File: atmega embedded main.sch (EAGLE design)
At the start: 148 parts, among them K1 SWITCH, K10 SWITCH, K11 SWITCH, K12 SWITCH, K13 SWITCH, K14 SWITCH, K15 SWITCH, K16 SWITCH, K17 SWITCH, K18 SWITCH, K19 SWITCH, K2 SWITCH, K20 SWITCH, K21 SWITCH, K22 SWITCH, K23 SWITCH, K24 SWITCH, K25 SWITCH, K26 SWITCH, K27 SWITCH, K28 SWITCH, K29 SWITCH, K3 SWITCH, K30 SWITCH, K31 SWITCH, K32 SWITCH, K33 SWITCH, K34 SWITCH, K35 SWITCH, K36 SWITCH, K37 SWITCH, K38 SWITCH, K39 SWITCH, K4 SWITCH, K40 SWITCH, K41 SWITCH, K42 SWITCH, K43 SWITCH, K44 SWITCH, K45 SWITCH, K46 SWITCH, K47 SWITCH, K48 SWITCH, K49 SWITCH, K5 SWITCH, K50 SWITCH, K51 SWITCH, K52 SWITCH, K53 SWITCH, K54 SWITCH, K55 SWITCH, K56 SWITCH, K57 SWITCH, K58 SWITCH, K59 SWITCH, K6 SWITCH, K60 SWITCH, K61 SWITCH, K62 SWITCH, K63 SWITCH, K64 SWITCH, K65 SWITCH, K66 SWITCH, K7 SWITCH, K8 SWITCH, K9 SWITCH, U1 ATMEGA32U4-AU, X1 XTAL_GND

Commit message: Replaced chip with Atmege328p and made some other adjustments to the schematic
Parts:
- removed D45: (no value), adafruit:DIODEDO-1N4148
- removed D63: (no value), adafruit:DIODESMA
- removed K60: SWITCH, keyboard_switch:SWITCH
- added C10, C9: 22p, adafruit:C-USC0805
- added CN2: (no value), adafruit:USBMINIB
- added D29: (no value), adafruit:DIODESMA
- added IC1: ATMEGA328PROUND, atmega328:ATMEGA328PROUND
- added R5: 10K, adafruit:R-US_M0805
- added R6, R7: 22, adafruit:R-US_M0805
- added SW2: (no value), adafruit:SWITCH_PUSHBUTTONSOFTTOUCHSMD_SJ
- added X2: XTAL_GND, adafruit:XTAL-4-3225
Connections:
- removed net N$43: D45.C, K24.P$2
- removed net N$65: D63.C, K60.P$2
- removed net N$80: D15.C, K47.P$2
- new net D+: CN2.D+, IC1.(PCI8/ADC0)PC0, R6.1, R6.2
- new net D-: CN2.D-, R7.2
- new net N$15: IC1.PC6(/RESET/PCI14), R5.2, SW2.P$2
- new net N$16: C9.1, IC1.PB6(XTAL1/TOSC1/PCI6), X2.X1
- new net N$17: C10.1, IC1.PB7(XTAL2/TOSC2/PCI7), X2.X2
- new net N$19: D15.C, K24.P$2
- new net N$20: D29.C, K47.P$2
- new net N$21: IC1.(PCI9/ADC1)PC1, R7.1
- new net N$22: CN2.ID
- net COL10: now also K62.P$1
- net COL13: no longer K60.P$1
- net COL14: no longer K47.P$1
- net COL3: no longer K24.P$1
- net COL6: now also K47.P$1
- net COL8: now also K24.P$1
- net COL9: no longer K62.P$1
- net GND: now also C10.2, C9.2, CN2.GND, IC1.AGND, IC1.GND, SW2.P$1, X2.G2
- net ROW1: now also D15.A, D29.A
- net ROW2: no longer D45.A, D63.A
- net ROW4: no longer D15.A
- net VCC: now also CN2.VBUS, IC1.AREF, IC1.AVCC, IC1.VCC, R5.1
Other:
- note added: "Floating ID pin means USB-B device"
- note added: "Reject, wrong chip"
- note added: "TODO: Regulate VCC with some condensers or something."
- moved on the sheet: C1, C2, C3, C4, C5, C6, C7, C8, CN1, D10, D11, D12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

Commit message: Added an alternative wiring with fake rows for a chip with fewer pins
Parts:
- added D100, D101, D102, D103, D104, D105, D106, D107, D108, D109, D110, D111, D112, D113, D114, D115, D116, D117, D118, D119, D120, D121, D122, D123, D124, D125, D126, D127, D128, D129, D130, D98, D99: (no value), adafruit:DIODESMA
- added D45, D63, D68, D69, D70, D71, D72, D73, D74, D75, D76, D77, D78, D79, D80, D81, D82, D83, D84, D85, D86, D87, D88, D89, D90, D91, D92, D93, D94, D95, D96, D97: (no value), adafruit:DIODEDO-1N4148
- added K100, K101, K102, K103, K104, K105, K106, K107, K108, K109, K110, K111, K112, K113, K114, K115, K116, K117, K118, K119, K120, K121, K122, K123, K124, K125, K126, K127, K128, K129, K130, K60, K67, K68, K69, K70, K71, K72, K73, K74, K75, K76, K77, K78, K79, K80, K81, K82, K83, K84, K85, K86, K87, K88, K89, K90, K91, K92, K93, K94, K95, K96, K97, K98, K99: SWITCH, keyboard_switch:SWITCH
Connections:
- new net N$100: D71.C, K71.P$2
- new net N$101: D74.C, K78.P$2
- new net N$102: D116.C, K98.P$1
- new net N$103: D117.C, K105.P$1
- new net N$104: D95.C, K85.P$2
- new net N$105: D94.C, K91.P$2
- new net N$106: D104.C, K128.P$2
- new net N$107: D86.C, K97.P$2
- new net N$108: D93.C, K90.P$2
- new net N$109: D92.C, K84.P$2
- new net N$110: D75.C, K77.P$2
- new net N$111: D115.C, K104.P$2
- new net N$112: D127.C, K123.P$2
- new net N$113: D111.C, K124.P$2
- new net N$114: D126.C, K121.P$2
- new net N$115: D120.C, K120.P$2
- new net N$116: D128.C, K117.P$2
- new net N$118: D114.C, K127.P$2
- new net N$119: D113.C, K126.P$2
- new net N$120: D112.C, K125.P$2
- new net N$121: D119.C, K119.P$2
- new net N$123: D99.C, K99.P$2
- new net N$124: D100.C, K100.P$2
- new net N$125: D101.C, K101.P$2
- new net N$126: D102.C, K102.P$2
- new net N$127: D103.C, K103.P$2
- new net N$130: D124.C, K116.P$2
- new net N$131: D123.C, K115.P$2
- new net N$132: D122.C, K114.P$2
- new net N$133: D121.C, K113.P$2
- new net N$134: D118.C, K112.P$2
- new net N$135: D109.C, K106.P$2
- new net N$136: D108.C, K107.P$2
- new net N$137: D107.C, K108.P$2
- new net N$138: D106.C, K109.P$2
- new net N$139: D105.C, K110.P$2
- new net N$141: D63.C, K67.P$2
- new net N$142: D125.C, K122.P$2
- new net N$143: D129.C, K129.P$1
- new net N$144: D130.C, K130.P$2
- new net N$151: D82.C, K93.P$1
- new net N$152: D81.C, K87.P$1
- new net N$153: D80.C, K80.P$1
- new net N$154: D105.A, D106.A, D107.A, D108.A, D109.A
- new net N$155: D100.A, D101.A, D102.A, D103.A, D99.A
- new net N$160: D87.A, D90.A, D93.A, D94.A
- new net N$161: D72.C, K72.P$2
- new net N$162: D73.C, K79.P$2
- new net N$163: D96.C, K86.P$2
- new net N$164: D97.C, K92.P$2
- new net N$23: D45.C, K60.P$1
- new net N$24: D83.C, K94.P$2
- new net N$25: D79.C, K73.P$1
- new net N$26: D118.A, D121.A, D122.A, D123.A, D124.A
- new net N$27: D98.C, K118.P$1
- new net N$28: D110.C, K111.P$1
- new net N$35: D78.C, K74.P$2
- new net N$43: D77.C, K75.P$2
- new net N$64: D68.C, K68.P$2
- new net N$65: D89.C, K82.P$2
- new net N$72: D88.C, K81.P$2
- new net N$80: D87.C, K88.P$2
- new net N$92: D84.C, K95.P$2
- new net N$93: D85.C, K96.P$2
- new net N$94: D90.C, K89.P$2
- new net N$95: D91.C, K83.P$2
- new net N$96: D76.C, K76.P$2
- new net N$97: D69.C, K69.P$2
- new net N$98: D70.C, K70.P$2
- new net ROW6: D104.A, D115.A, D127.A, D128.A, D45.A, D79.A, D80.A, D81.A, D82.A
- new net ROW7: D110.A, D116.A, D117.A, D72.A, D73.A, D96.A, D97.A, D98.A
- net COL10: now also K100.P$1, K107.P$1, K111.P$2, K113.P$1, K120.P$1, K124.P$1, K128.P$1
- net COL11: now also K101.P$1, K105.P$2, K108.P$1, K114.P$1, K121.P$1, K123.P$1, K125.P$1
- net COL12: now also K102.P$1, K109.P$1, K115.P$1, K117.P$1, K122.P$1, K126.P$1, K98.P$2
- net COL13: now also K103.P$1, K104.P$1, K110.P$1, K116.P$1, K127.P$1
- net COL2: now also K60.P$2, K67.P$1, K74.P$1, K81.P$1, K88.P$1, K94.P$1
- net COL3: now also K68.P$1, K72.P$1, K73.P$2, K75.P$1, K82.P$1, K95.P$1
- net COL4: now also K69.P$1, K76.P$1, K79.P$1, K80.P$2, K83.P$1, K89.P$1, K96.P$1
- net COL5: now also K70.P$1, K77.P$1, K84.P$1, K86.P$1, K87.P$2, K90.P$1, K97.P$1
- net COL6: now also K130.P$1, K71.P$1, K78.P$1, K85.P$1, K91.P$1, K92.P$1, K93.P$2
- net COL9: now also K106.P$1, K112.P$1, K118.P$2, K119.P$1, K129.P$2, K99.P$1
- net ROW1: now also D63.A, D68.A, D69.A, D70.A, D71.A
- net ROW2: now also D74.A, D75.A, D76.A, D77.A, D78.A
- net ROW3: now also D88.A, D89.A, D91.A, D92.A, D95.A
- net ROW4: now also D119.A, D120.A, D125.A, D126.A
- net ROW5: now also D111.A, D112.A, D113.A, D114.A, D129.A, D130.A, D83.A, D84.A, D85.A, D86.A
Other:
- moved on the sheet: C1, C2, C8, CN1, R1, R2, R3, R4, SW1, U1, X1

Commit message: Traced stuff
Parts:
- removed C1, C2: 22p, adafruit:C-USC0805
- removed C8: 1u, adafruit:C-USC0805
- removed CN1, CN2: (no value), adafruit:USBMINIB
- removed D1, D2, D22, D23, D24, D25, D26, D27, D28, D3, D30, D31, D32, D33, D34, D35, D36, D4, D42, D43, D44, D46, D47, D48, D49, D5, D50, D51, D52, D53, D6, D7: (no value), adafruit:DIODEDO-1N4148
- removed D10, D11, D12, D13, D14, D15, D16, D17, D18, D19, D20, D21, D29, D37, D38, D39, D40, D41, D54, D55, D56, D57, D58, D59, D60, D61, D62, D64, D65, D66, D67, D8, D9: (no value), adafruit:DIODESMA
- removed K1, K10, K11, K12, K13, K14, K15, K16, K17, K18, K19, K2, K20, K21, K22, K23, K24, K25, K26, K27, K28, K29, K3, K30, K31, K32, K33, K34, K35, K36, K37, K38, K39, K4, K40, K41, K42, K43, K44, K45, K46, K47, K48, K49, K5, K50, K51, K52, K53, K54, K55, K56, K57, K58, K59, K6, K61, K62, K63, K64, K65, K66, K7, K8, K9: SWITCH, keyboard_switch:SWITCH
- removed R1, R2: 10K, adafruit:R-US_M0805
- removed R3, R4: 22, adafruit:R-US_M0805
- removed SW1, SW2: (no value), adafruit:SWITCH_PUSHBUTTONSOFTTOUCHSMD_SJ
- removed X1, X2: XTAL_GND, adafruit:XTAL-4-3225
- added Q1: (no value), crystal:CRYSTALHC49S
- added S1: (no value), switch-omron:10-XX
- D45, D63, D68, D69, D70, D71, D72, D73, D74, D75, D76, D77, D78, D79, D80, D81, D82, D83, D84, D85, D86, D87, D88, D89, D90, D91, D92, D93, D94, D95, D96, D97: device adafruit:DIODEDO-1N4148 -> adafruit:DIODESMA
- U1: value ATMEGA32U4-AU -> (none); device adafruit:ATMEGA32U4-AU -> microusb:USB""
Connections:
- removed net COL11: K101.P$1, K105.P$2, K108.P$1, K114.P$1, K121.P$1, K123.P$1, K125.P$1, K37.P$1, K44.P$1, K51.P$1, K58.P$1, K63.P$1, U1.PB7(OC0A/OC1C/RTS)
- removed net COL12: K102.P$1, K109.P$1, K115.P$1, K117.P$1, K122.P$1, K126.P$1, K38.P$1, K45.P$1, K52.P$1, K59.P$1, K64.P$1, K98.P$2, U1.PF7(ADC7(TDI)
- removed net COL13: K103.P$1, K104.P$1, K110.P$1, K116.P$1, K127.P$1, K39.P$1, K46.P$1, K53.P$1, K65.P$1, U1.PF6(ADC6/TDO)
- removed net COL14: K40.P$1, K54.P$1, K61.P$1, K66.P$1, U1.PF5(ADC5/TMS)
- removed net N$1 (its old number): C1.1, U1.XTAL1, X1.X1
- removed net N$100: D71.C, K71.P$2
- removed net N$101: D74.C, K78.P$2
- removed net N$102: D116.C, K98.P$1
- removed net N$103: D117.C, K105.P$1
- removed net N$104: D95.C, K85.P$2
- removed net N$105: D94.C, K91.P$2
- removed net N$107: D86.C, K97.P$2
- removed net N$108: D93.C, K90.P$2
- removed net N$109: D92.C, K84.P$2
- removed net N$110: D75.C, K77.P$2
- removed net N$113: D111.C, K124.P$2
- removed net N$114: D126.C, K121.P$2
- removed net N$115: D120.C, K120.P$2
- removed net N$118: D114.C, K127.P$2
- removed net N$119: D113.C, K126.P$2
- removed net N$120: D112.C, K125.P$2
- removed net N$121: D119.C, K119.P$2
- removed net N$123: D99.C, K99.P$2
- removed net N$124: D100.C, K100.P$2
- removed net N$125: D101.C, K101.P$2
- removed net N$126: D102.C, K102.P$2
- removed net N$127: D103.C, K103.P$2
- removed net N$130: D124.C, K116.P$2
- removed net N$131: D123.C, K115.P$2
- removed net N$132: D122.C, K114.P$2
- removed net N$133: D121.C, K113.P$2
- removed net N$134: D118.C, K112.P$2
- removed net N$135: D109.C, K106.P$2
- removed net N$136: D108.C, K107.P$2
- removed net N$137: D107.C, K108.P$2
- removed net N$138: D106.C, K109.P$2
- removed net N$139: D105.C, K110.P$2
- removed net N$141: D63.C, K67.P$2
- removed net N$144: D130.C, K130.P$2
- removed net N$154: D105.A, D106.A, D107.A, D108.A, D109.A
- removed net N$155: D100.A, D101.A, D102.A, D103.A, D99.A
- removed net N$160: D87.A, D90.A, D93.A, D94.A
- removed net N$161: D72.C, K72.P$2
- removed net N$162: D73.C, K79.P$2
- removed net N$163: D96.C, K86.P$2
- removed net N$164: D97.C, K92.P$2
- removed net N$2 (its old number): C2.1, U1.XTAL2, X1.X2
- removed net N$26 (its old number): D118.A, D121.A, D122.A, D123.A, D124.A
- removed net N$3 (its old number): R1.2, SW1.P$2, U1./RESET
- removed net N$4 (its old number): R2.2, U1.PE2(!HWB)
- removed net N$42: D34.C, K31.P$2
- removed net N$5 (its old number): CN1.D+, R3.1
- removed net N$65 (its old number): D89.C, K82.P$2
- removed net N$66 (its old number): D67.C, K61.P$2
- removed net N$67 (its old number): D41.C, K66.P$2
- removed net N$68 (its old number): D40.C, K65.P$2
- removed net N$69: D39.C, K64.P$2
- removed net N$70: D38.C, K63.P$2
- removed net N$71: D57.C, K56.P$2
- removed net N$72: D88.C, K81.P$2
- removed net N$73: D21.C, K41.P$2
- removed net N$74: D9.C, K35.P$2
- removed net N$75: D10.C, K36.P$2
- removed net N$76: D11.C, K37.P$2
- removed net N$77: D12.C, K38.P$2
- removed net N$78: D13.C, K39.P$2
- removed net N$79: D14.C, K40.P$2
- removed net N$81: D66.C, K54.P$2
- removed net N$82: D62.C, K53.P$2
- removed net N$83: D61.C, K52.P$2
- removed net N$84: D60.C, K51.P$2
- removed net N$85: D59.C, K50.P$2
- removed net N$86: D56.C, K49.P$2
- removed net N$87: D20.C, K42.P$2
- removed net N$88: D19.C, K43.P$2
- removed net N$89: D18.C, K44.P$2
- removed net N$90: D17.C, K45.P$2
- removed net N$91: D16.C, K46.P$2
- removed net N$92: D84.C, K95.P$2
- removed net N$93: D85.C, K96.P$2
- removed net N$94: D90.C, K89.P$2
- removed net N$95: D91.C, K83.P$2
- removed net N$96: D76.C, K76.P$2
- removed net N$97: D69.C, K69.P$2
- removed net N$98: D70.C, K70.P$2
- new net N$23: D86.C, K97.P$1
- new net N$25: D75.C, K77.P$1
- net COL1: now also K60.P$2, K67.P$2, K74.P$2, K81.P$2, K88.P$2, K94.P$2; no longer K1.P$1, K15.P$1, K22.P$1, K29.P$1, K8.P$1, U1.PD5(XCK/CTS)
- net COL10: now also K103.P$2, K104.P$1, K110.P$2, K116.P$2, K127.P$2; no longer K100.P$1, K107.P$1, K111.P$2, K113.P$1, K120.P$1, K124.P$1, K128.P$1, K36.P$1, K43.P$1, K50.P$1, K57.P$1, K62.P$1, U1.PB6(OC1B/OC4B/ADC13)
- net COL2: now also K68.P$2, K72.P$2, K73.P$2, K75.P$2, K82.P$2, K95.P$2; no longer K16.P$1, K2.P$1, K23.P$1, K30.P$1, K60.P$2, K67.P$1, K74.P$1, K81.P$1, K88.P$1, K9.P$1, K94.P$1, U1.PD3(INT3/TXD1)
- net COL3: now also K69.P$2, K76.P$2, K79.P$2, K80.P$2, K83.P$2, K89.P$2, K96.P$2; no longer K10.P$1, K17.P$1, K3.P$1, K31.P$1, K68.P$1, K72.P$1, K73.P$2, K75.P$1, K82.P$1, K95.P$1, U1.PD2(INT2/RXD1)
- net COL4: now also K70.P$2, K77.P$2, K84.P$2, K86.P$2, K87.P$2, K90.P$2, K97.P$2; no longer K11.P$1, K18.P$1, K25.P$1, K32.P$1, K4.P$1, K69.P$1, K76.P$1, K79.P$1, K80.P$2, K83.P$1, K89.P$1, K96.P$1, U1.PB0(SS)
- net COL5: now also K130.P$2, K71.P$2, K78.P$2, K85.P$2, K91.P$2, K92.P$2, K93.P$2; no longer K12.P$1, K19.P$1, K26.P$1, K33.P$1, K5.P$1, K70.P$1, K77.P$1, K84.P$1, K86.P$1, K87.P$2, K90.P$1, K97.P$1, U1.PB1(SCK)
- net COL6: now also K106.P$2, K112.P$2, K118.P$1, K119.P$2, K129.P$2, K99.P$2; no longer K13.P$1, K130.P$1, K20.P$1, K27.P$1, K47.P$1, K6.P$1, K71.P$1, K78.P$1, K85.P$1, K91.P$1, K92.P$1, K93.P$2, U1.PB2(PDI/MOSI)
- net COL7: now also K100.P$2, K107.P$2, K111.P$1, K113.P$2, K120.P$2, K124.P$2, K128.P$1; no longer K14.P$1, K21.P$1, K28.P$1, K7.P$1, U1.PB3(PDO/MISO)
- net COL8: now also K101.P$2, K105.P$1, K108.P$2, K114.P$2, K121.P$2, K123.P$1, K125.P$2; no longer K24.P$1, K34.P$1, K41.P$1, K48.P$1, K55.P$1, U1.PD1(INT1/SDA)
- net COL9: now also K102.P$2, K109.P$2, K115.P$2, K117.P$1, K122.P$2, K126.P$2, K98.P$1; no longer K106.P$1, K112.P$1, K118.P$2, K119.P$1, K129.P$2, K35.P$1, K42.P$1, K49.P$1, K56.P$1, K99.P$1, U1.PD0(INT0/OC0B/SCL)
- net D+: now also U1.D+; no longer CN2.D+
- net D-: now also U1.D-; no longer CN2.D-
- net GND: now also S1.P1; no longer C1.2, C2.2, C8.1, CN1.GND, CN2.GND, R2.1, SW1.P$1, SW2.P$1, U1.GND1, U1.GND2, U1.GND3, U1.UGND, X1.G2, X2.G2
- net N$10: now also D77.C, K75.P$1; no longer D49.C, K26.P$2
- net N$11: now also D89.C, K82.P$1; no longer D48.C, K19.P$2
- net N$12: now also D68.C, K68.P$1; no longer D24.C, K12.P$2
- net N$13: now also D84.C, K95.P$1; no longer D8.C, K34.P$2
- net N$14: now also D76.C, K76.P$1; no longer D2.C, K2.P$2
- net N$142: now also K122.P$1; no longer K122.P$2
- net N$15: now also S1.S, S1.S1; no longer SW2.P$2
- net N$16: now also Q1.2; no longer X2.X1
- net N$17: now also Q1.1; no longer X2.X2
- net N$18: now also D69.C, K69.P$1; no longer D64.C, K59.P$2
- net N$19: now also D90.C, K89.P$1; no longer D15.C, K24.P$2
- net N$20: now also D85.C, K96.P$1; no longer D29.C, K47.P$2
- net N$22: now also D91.C, K83.P$1; no longer CN2.ID
- net N$24: now also D70.C, K70.P$1; no longer D83.C, K94.P$2
- net N$27: now also K118.P$2; no longer K118.P$1
- net N$28: now also K111.P$2; no longer K111.P$1
- net N$29: now also D92.C, K84.P$1; no longer D32.C, K29.P$2
- net N$30: now also D93.C, K90.P$1; no longer D33.C, K30.P$2
- net N$31: now also D94.C, K91.P$1; no longer D31.C, K22.P$2
- net N$32: now also D71.C, K71.P$1; no longer D30.C, K15.P$2
- net N$33: now also D74.C, K78.P$1; no longer D28.C, K8.P$2
- net N$34: now also D95.C, K85.P$1; no longer D1.C, K1.P$2
- net N$35: now also D130.C, K130.P$1; no longer D78.C, K74.P$2
- net N$36: now also D72.C, K72.P$1; no longer D27.C, K9.P$2
- net N$37: now also D73.C, K79.P$1; no longer D26.C, K10.P$2
- net N$38: now also D96.C, K86.P$1; no longer D3.C, K3.P$2
- net N$39: now also D97.C, K92.P$1; no longer D44.C, K17.P$2
- net N$40: now also D117.C, K105.P$2; no longer D43.C, K16.P$2
- net N$41: now also D116.C, K98.P$2; no longer D42.C, K23.P$2
- net N$43: now also D119.C, K119.P$1; no longer D77.C, K75.P$2
- net N$44: now also D99.C, K99.P$1; no longer D35.C, K32.P$2
- net N$45: now also D109.C, K106.P$1; no longer D46.C, K25.P$2
- net N$46: now also D118.C, K112.P$1; no longer D47.C, K18.P$2
- net N$47: now also D111.C, K124.P$1; no longer D25.C, K11.P$2
- net N$48: now also D100.C, K100.P$1; no longer D4.C, K4.P$2
- net N$49: now also D108.C, K107.P$1; no longer D5.C, K5.P$2
- net N$50: now also D121.C, K113.P$1; no longer D7.C, K7.P$2
- net N$51: now also D120.C, K120.P$1; no longer D6.C, K6.P$2
- net N$52: now also D126.C, K121.P$1; no longer D23.C, K13.P$2
- net N$53: now also D101.C, K101.P$1; no longer D22.C, K14.P$2
- net N$54: now also D107.C, K108.P$1; no longer D52.C, K21.P$2
- net N$55: now also D122.C, K114.P$1; no longer D51.C, K20.P$2
- net N$56: now also D112.C, K125.P$1; no longer D50.C, K27.P$2
- net N$57: now also D123.C, K115.P$1; no longer D53.C, K28.P$2
- net N$58: now also D106.C, K109.P$1; no longer D54.C, K55.P$2
- net N$59: now also D102.C, K102.P$1; no longer D55.C, K48.P$2
- net N$6: now also D63.C, K67.P$1; no longer CN1.D-, R4.1
- net N$60: now also D113.C, K126.P$1; no longer D36.C, K33.P$2
- net N$61: now also D124.C, K116.P$1; no longer D37.C, K62.P$2
- net N$62: now also D105.C, K110.P$1; no longer D65.C, K58.P$2
- net N$63: now also D103.C, K103.P$1; no longer D58.C, K57.P$2
- net N$64: now also D114.C, K127.P$1; no longer D68.C, K68.P$2
- net N$7: now also D88.C, K81.P$1; no longer R4.2, U1.D-
- net N$8: now also D78.C, K74.P$1; no longer R3.2, U1.D+
- net N$80: now also K88.P$1; no longer K88.P$2
- net N$9: now also D83.C, K94.P$1; no longer C8.2, U1.UCAP
- net ROW1: now also D100.A, D101.A, D102.A, D103.A, D99.A; no longer D15.A, D29.A, D32.A, D33.A, D34.A, D35.A, D36.A, D37.A, D38.A, D39.A, D40.A, D41.A, U1.PB5(OC1A/ADC12/!OC4B)
- net ROW2: now also D105.A, D106.A, D107.A, D108.A, D109.A; no longer D31.A, D42.A, D46.A, D49.A, D50.A, D53.A, D54.A, D57.A, D58.A, D64.A, D65.A, D67.A, U1.PB4(ADC11)
- net ROW3: now also D118.A, D121.A, D122.A, D123.A, D124.A; no longer D30.A, D43.A, D44.A, D47.A, D48.A, D51.A, D52.A, D55.A, D56.A, D59.A, D60.A, D61.A, D62.A, D66.A, U1.PD7(OC4D/ADC10/T0)
- net ROW4: now also D87.A, D90.A, D93.A, D94.A; no longer D16.A, D17.A, D18.A, D19.A, D20.A, D21.A, D22.A, D23.A, D24.A, D25.A, D26.A, D27.A, D28.A, U1.PD6(T1/ADC9/!OC4D)
- net ROW5: no longer D1.A, D10.A, D11.A, D12.A, D13.A, D14.A, D2.A, D3.A, D4.A, D5.A, D6.A, D7.A, D8.A, D9.A, U1.PD4(ICP1/ADC8)
- net VCC: now also U1.VBUS; no longer CN1.VBUS, CN2.VBUS, R1.1, U1.AVCC, U1.AVCC1, U1.UVCC, U1.VCC, U1.VCC1
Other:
- note removed: "Reject, wrong chip"
- note removed: "TODO: Regulate VCC with some condensers or something."
- moved on the sheet: D100, D101, D102, D103, D104, D105, D106, D107, D108, D109, D110, D111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

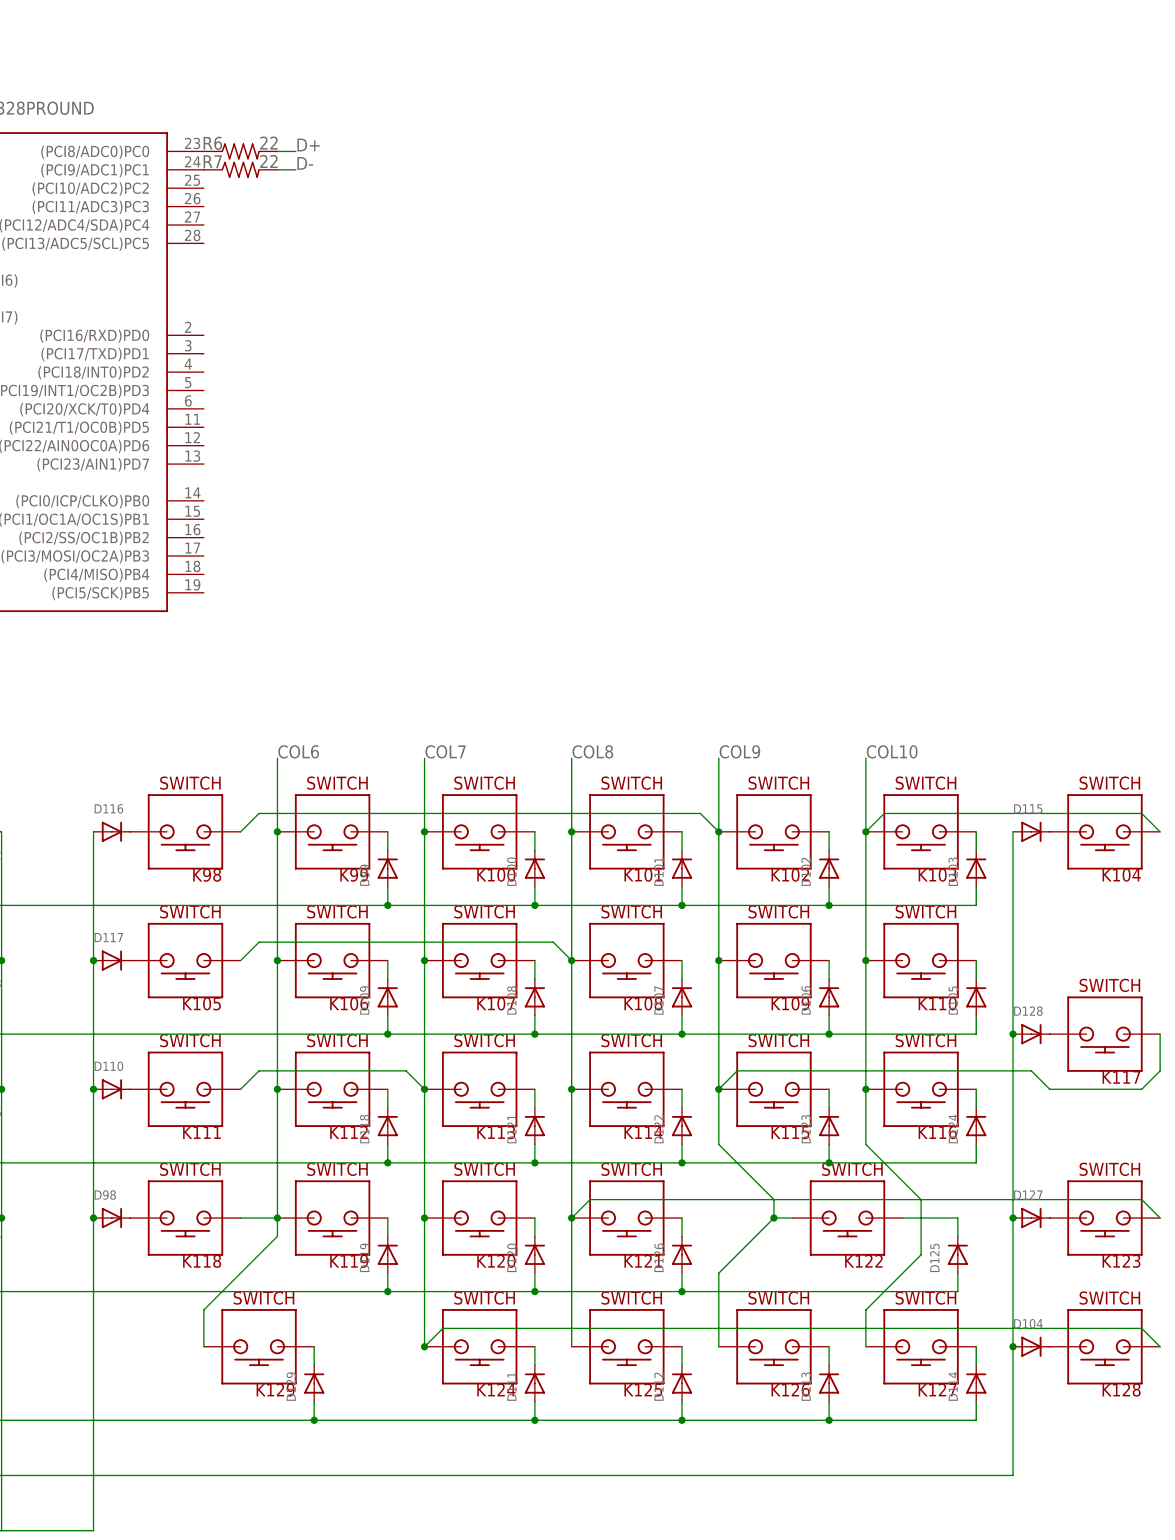
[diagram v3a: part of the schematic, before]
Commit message: Flipped switches and rewired everything
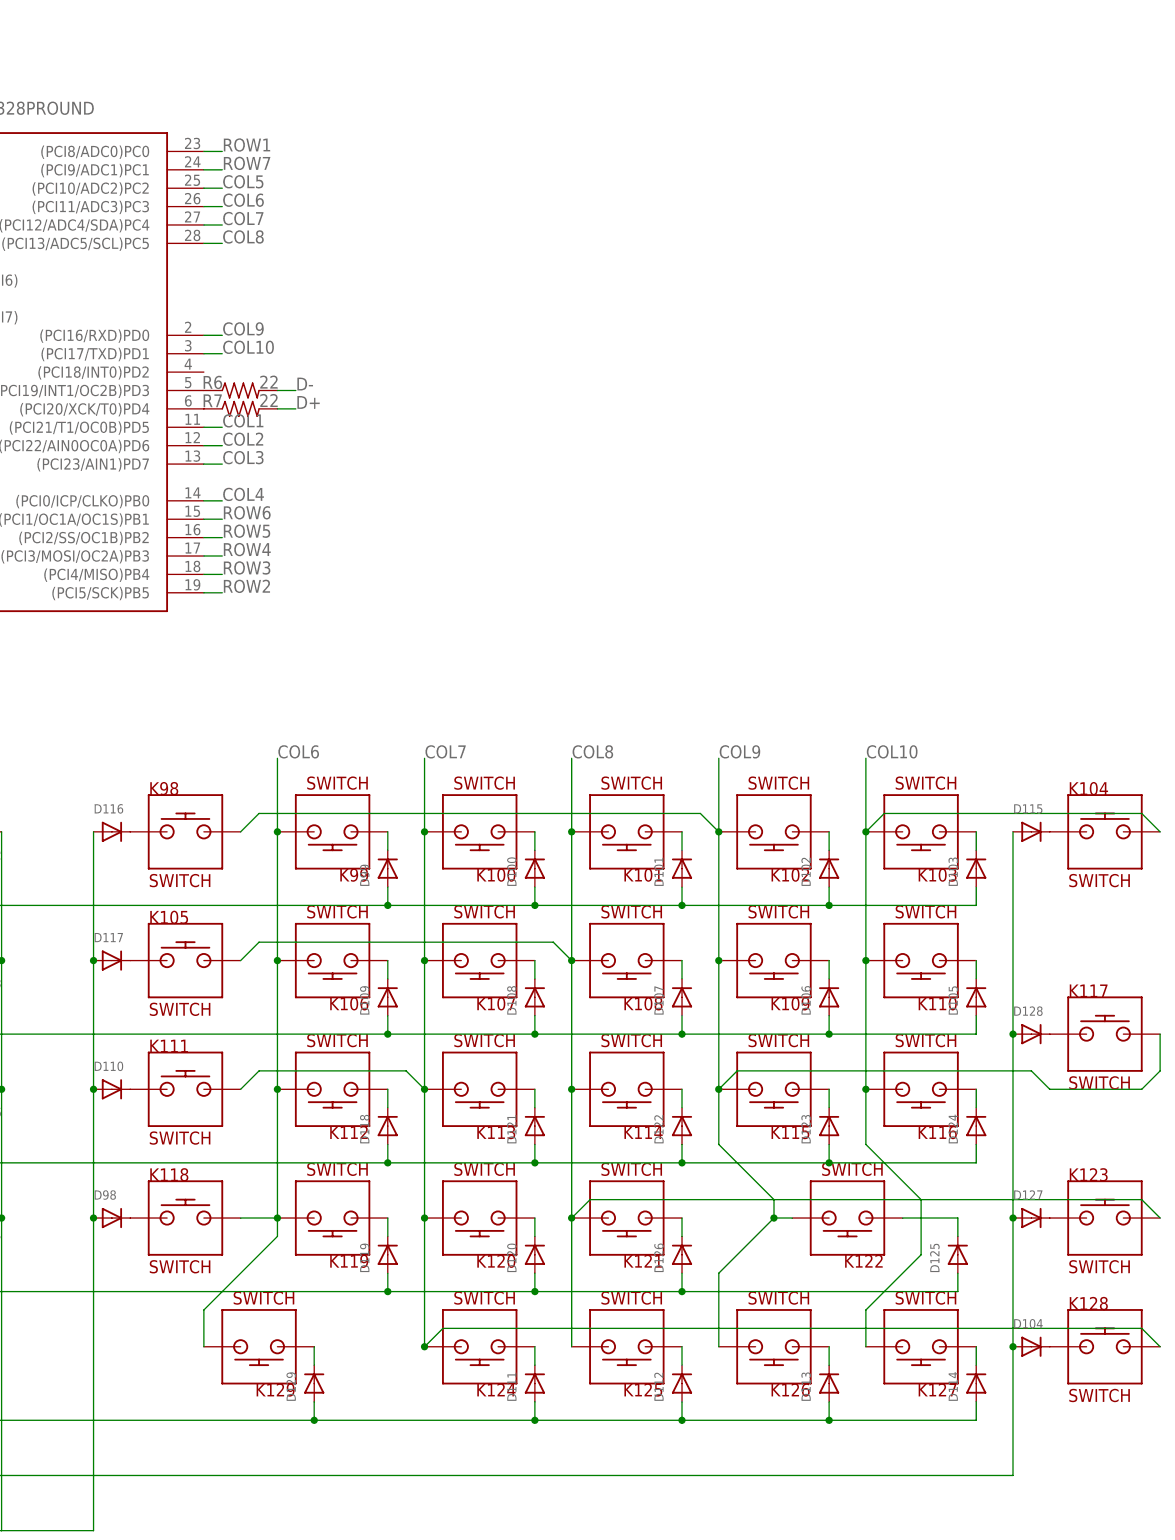
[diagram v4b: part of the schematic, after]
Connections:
- new net N$42: D115.C, K104.P$1
- net COL1: now also IC1.(PCI21/T1/OC0B)PD5
- net COL10: now also IC1.(PCI17/TXD)PD1, K104.P$2; no longer K104.P$1
- net COL2: now also IC1.(PCI22/AIN0OC0A)PD6
- net COL3: now also IC1.(PCI23/AIN1)PD7
- net COL4: now also IC1.(PCI0/ICP/CLKO)PB0
- net COL5: now also IC1.(PCI10/ADC2)PC2
- net COL6: now also IC1.(PCI11/ADC3)PC3, K118.P$2; no longer K118.P$1
- net COL7: now also IC1.(PCI12/ADC4/SDA)PC4, K111.P$2, K128.P$2; no longer K111.P$1, K128.P$1
- net COL8: now also IC1.(PCI13/ADC5/SCL)PC5, K105.P$2, K123.P$2; no longer K105.P$1, K123.P$1
- net COL9: now also IC1.(PCI16/RXD)PD0, K117.P$2, K98.P$2; no longer K117.P$1, K98.P$1
- net D+: now also R7.2; no longer IC1.(PCI8/ADC0)PC0, R6.1, R6.2
- net D-: now also R6.2; no longer R7.2
- net N$21: now also IC1.(PCI20/XCK/T0)PD4; no longer IC1.(PCI9/ADC1)PC1
- net N$27: now also D116.C, K98.P$1; no longer D98.C, K118.P$2
- net N$28: now also D117.C, K105.P$1; no longer D110.C, K111.P$2
- net N$40: now also D110.C, K111.P$1; no longer D117.C, K105.P$2
- net N$41: now also D98.C, K118.P$1; no longer D116.C, K98.P$2
- net N$65: now also D128.C, K117.P$1; no longer D115.C, K104.P$2
- net N$66: now also D127.C, K123.P$1; no longer D128.C, K117.P$2
- net N$67: now also D104.C, K128.P$1; no longer D127.C, K123.P$2
- net N$68: now also IC1.(PCI19/INT1/OC2B)PD3, R6.1; no longer D104.C, K128.P$2
- net ROW1: now also IC1.(PCI8/ADC0)PC0
- net ROW2: now also IC1.(PCI5/SCK)PB5
- net ROW3: now also IC1.(PCI4/MISO)PB4
- net ROW4: now also IC1.(PCI3/MOSI/OC2A)PB3
- net ROW5: now also IC1.(PCI2/SS/OC1B)PB2
- net ROW6: now also IC1.(PCI1/OC1A/OC1S)PB1
- net ROW7: now also IC1.(PCI9/ADC1)PC1
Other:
- moved on the sheet: K104, K105, K111, K117, K118, K123, K128, K98, R6, R7
